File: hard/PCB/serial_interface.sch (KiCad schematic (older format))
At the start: 19 parts

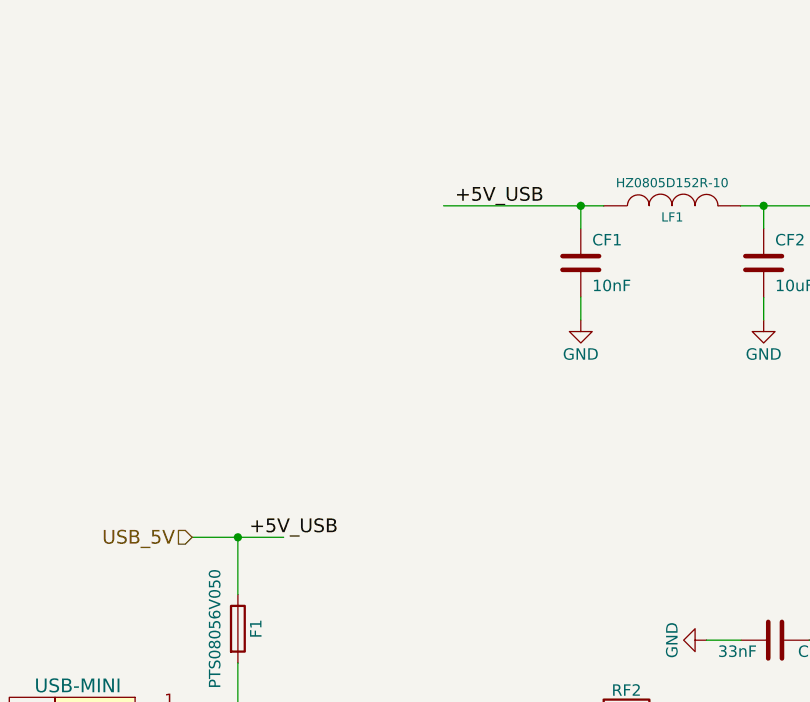
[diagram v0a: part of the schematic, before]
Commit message: se modifican el pin hdmi- las resitencias RN1 - eñ conector de  voltaje
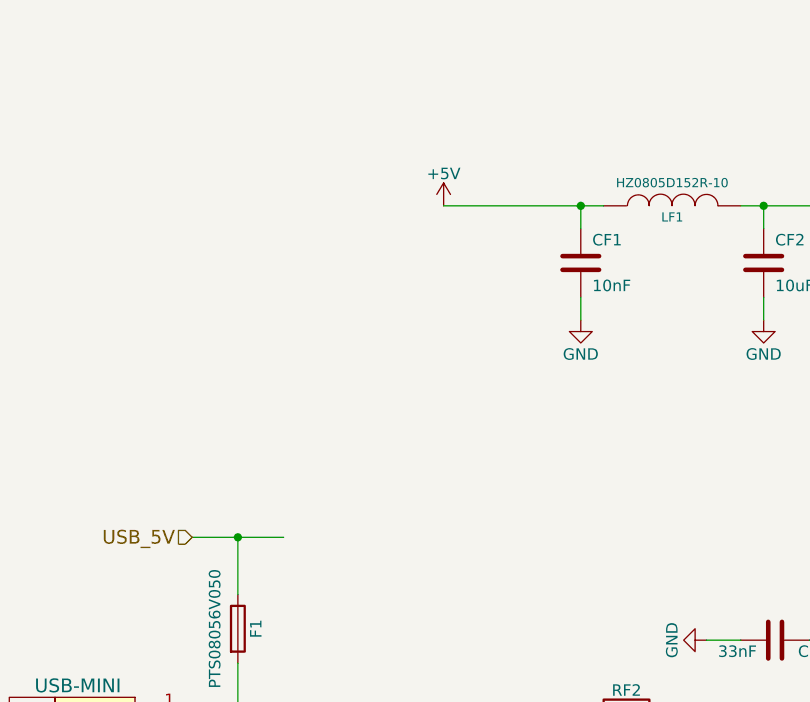
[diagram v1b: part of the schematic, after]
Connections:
- net labels added: +5V
- net labels removed: +5V_USB
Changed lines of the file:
@@
 Wire Wire Line
 	4750 3850 5150 3850
-Text Label 5000 3850 0    60   ~ 0
-+5V_USB
-Text Label 5900 2400 0    60   ~ 0
-+5V_USB
-Wire Wire Line
-	5850 2400 6550 2400
 $Comp
 L Fuse F1
@@
 Wire Wire Line
 	7600 6300 7400 6300
-Text Label 6800 6300 0    60   ~ 0
-+5VA
 Wire Wire Line
 	7600 5400 7200 5400
@@
 	0    1    1    0
 $EndComp
+Wire Wire Line
+	5850 2400 6550 2400
+$Comp
+L +5V #PWR019
+U 1 1 595DA814
+P 5850 2400
+F 0 "#PWR019" H 5850 2250 50  0001 C CNN
+F 1 "+5V" H 5850 2540 50  0000 C CNN
+F 2 "" H 5850 2400 50  0000 C CNN
+F 3 "" H 5850 2400 50  0000 C CNN
+	1    5850 2400
+	1    0    0    -1
+$EndComp
+Text Label 6800 6300 0    60   ~ 0
++5VA
 $EndSCHEMATC

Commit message: Changes in HDMISpartan6_Board
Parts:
- CF5, CF6: value 47pF -> 15pF
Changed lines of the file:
@@
 $Descr A3 16535 11693
 encoding utf-8
-Sheet 2 5
+Sheet 2 6
 Title ""
 Date "9 aug 2012"
@@
 P 5950 5500
 F 0 "CF5" H 6000 5600 50  0000 L CNN
-F 1 "47pF" V 6050 5250 50  0000 L CNN
+F 1 "15pF" V 6050 5250 50  0000 L CNN
 F 2 "Capacitors_SMD:C_0603" H 5950 5500 60  0001 C CNN
 F 3 "" H 5950 5500 60  0001 C CNN
@@
 P 5950 6100
 F 0 "CF6" H 6000 6200 50  0000 L CNN
-F 1 "47pF" V 6050 5850 50  0000 L CNN
+F 1 "15pF" V 6050 5850 50  0000 L CNN
 F 2 "Capacitors_SMD:C_0603" H 5950 6100 60  0001 C CNN
 F 3 "" H 5950 6100 60  0001 C CNN
@@
 $EndComp
 $Comp
-L +3V3 #PWR06
+L +3V3 #PWR010
 U 1 1 589F5460
 P 10300 6750
-F 0 "#PWR06" H 10300 6600 50  0001 C CNN
+F 0 "#PWR010" H 10300 6600 50  0001 C CNN
 F 1 "+3V3" H 10300 6890 50  0000 C CNN
 F 2 "" H 10300 6750 50  0000 C CNN
@@
 $EndComp
 $Comp
-L +3V3 #PWR07
+L +3V3 #PWR011
 U 1 1 589F5F40
 P 10300 5050
-F 0 "#PWR07" H 10300 4900 50  0001 C CNN
+F 0 "#PWR011" H 10300 4900 50  0001 C CNN
 F 1 "+3V3" H 10300 5190 50  0000 C CNN
 F 2 "" H 10300 5050 50  0000 C CNN
@@
 $EndComp
 $Comp
-L +3V3 #PWR08
+L +3V3 #PWR012
 U 1 1 589F6257
 P 10500 4800
-F 0 "#PWR08" H 10500 4650 50  0001 C CNN
+F 0 "#PWR012" H 10500 4650 50  0001 C CNN
 F 1 "+3V3" H 10500 4940 50  0000 C CNN
 F 2 "" H 10500 4800 50  0000 C CNN
@@
 $EndComp
 $Comp
-L +3V3 #PWR09
+L +3V3 #PWR013
 U 1 1 589F6BB3
 P 8800 3450
-F 0 "#PWR09" H 8800 3300 50  0001 C CNN
+F 0 "#PWR013" H 8800 3300 50  0001 C CNN
 F 1 "+3V3" H 8800 3590 50  0000 C CNN
 F 2 "" H 8800 3450 50  0000 C CNN
@@
 Wire Wire Line
 	7600 6400 7450 6400
-Connection ~ 8500 3450
-Wire Wire Line
-	8600 3700 8600 3450
-Wire Wire Line
-	8600 3450 8500 3450
 Wire Wire Line
 	8300 2900 8300 3700
@@
 Wire Wire Line
 	5050 4800 4800 4800
-Wire Wire Line
-	4800 5000 5000 5000
-Wire Wire Line
-	5000 5000 5000 5050
 Wire Wire Line
 	3650 4650 3650 5050
@@
 	6450 2500 6450 2400
 $Comp
-L GND #PWR010
+L GND #PWR014
 U 1 1 58A66750
 P 6450 2900
-F 0 "#PWR010" H 6450 2650 50  0001 C CNN
+F 0 "#PWR014" H 6450 2650 50  0001 C CNN
 F 1 "GND" H 6450 2750 50  0000 C CNN
 F 2 "" H 6450 2900 50  0000 C CNN
@@
 	7100 6300 6750 6300
 $Comp
-L GND #PWR011
+L GND #PWR015
 U 1 1 58A8D1C3
 P 7250 2900
-F 0 "#PWR011" H 7250 2650 50  0001 C CNN
+F 0 "#PWR015" H 7250 2650 50  0001 C CNN
 F 1 "GND" H 7250 2750 50  0000 C CNN
 F 2 "" H 7250 2900 50  0000 C CNN
@@
 $EndComp
 $Comp
-L GND #PWR012
+L GND #PWR016
 U 1 1 58A8D267
 P 7900 3350
-F 0 "#PWR012" H 7900 3100 50  0001 C CNN
+F 0 "#PWR016" H 7900 3100 50  0001 C CNN
 F 1 "GND" H 7900 3200 50  0000 C CNN
 F 2 "" H 7900 3350 50  0000 C CNN
@@
 $EndComp
 $Comp
-L GND #PWR013
+L GND #PWR017
 U 1 1 58A8D7DD
 P 8300 7400
-F 0 "#PWR013" H 8300 7150 50  0001 C CNN
+F 0 "#PWR017" H 8300 7150 50  0001 C CNN
 F 1 "GND" H 8300 7250 50  0000 C CNN
 F 2 "" H 8300 7400 50  0000 C CNN
@@
 $EndComp
 $Comp
-L GND #PWR014
+L GND #PWR018
 U 1 1 58A8DF8B
 P 7450 6450
-F 0 "#PWR014" H 7450 6200 50  0001 C CNN
+F 0 "#PWR018" H 7450 6200 50  0001 C CNN
 F 1 "GND" H 7450 6300 50  0000 C CNN
 F 2 "" H 7450 6450 50  0000 C CNN
@@
 $EndComp
 $Comp
-L GND #PWR015
+L GND #PWR019
 U 1 1 58A8E746
 P 5650 5900
-F 0 "#PWR015" H 5650 5650 50  0001 C CNN
+F 0 "#PWR019" H 5650 5650 50  0001 C CNN
 F 1 "GND" H 5650 5750 50  0000 C CNN
 F 2 "" H 5650 5900 50  0000 C CNN
@@
 $EndComp
 $Comp
-L GND #PWR016
+L GND #PWR020
 U 1 1 58A8EFD2
-P 5000 5050
-F 0 "#PWR016" H 5000 4800 50  0001 C CNN
-F 1 "GND" H 5000 4900 50  0000 C CNN
-F 2 "" H 5000 5050 50  0000 C CNN
-F 3 "" H 5000 5050 50  0000 C CNN
-	1    5000 5050
-	1    0    0    -1
-$EndComp
-$Comp
-L GND #PWR017
+P 4950 5050
+F 0 "#PWR020" H 4950 4800 50  0001 C CNN
+F 1 "GND" H 4950 4900 50  0000 C CNN
+F 2 "" H 4950 5050 50  0000 C CNN
+F 3 "" H 4950 5050 50  0000 C CNN
+	1    4950 5050
+	1    0    0    -1
+$EndComp
+$Comp
+L GND #PWR021
 U 1 1 58A8F696
 P 3650 5050
-F 0 "#PWR017" H 3650 4800 50  0001 C CNN
+F 0 "#PWR021" H 3650 4800 50  0001 C CNN
 F 1 "GND" H 3650 4900 50  0000 C CNN
 F 2 "" H 3650 5050 50  0000 C CNN
@@
 $EndComp
 $Comp
-L GND #PWR018
+L GND #PWR022
 U 1 1 58A8F991
 P 7000 4300
-F 0 "#PWR018" H 7000 4050 50  0001 C CNN
+F 0 "#PWR022" H 7000 4050 50  0001 C CNN
 F 1 "GND" H 7000 4150 50  0000 C CNN
 F 2 "" H 7000 4300 50  0000 C CNN
@@
 	5850 2400 6550 2400
 $Comp
-L +5V #PWR019
+L +5V #PWR023
 U 1 1 595DA814
 P 5850 2400
-F 0 "#PWR019" H 5850 2250 50  0001 C CNN
+F 0 "#PWR023" H 5850 2250 50  0001 C CNN
 F 1 "+5V" H 5850 2540 50  0000 C CNN
 F 2 "" H 5850 2400 50  0000 C CNN
@@
 Text Label 6800 6300 0    60   ~ 0
 +5VA
+Wire Wire Line
+	4950 5050 4950 5000
+Wire Wire Line
+	4950 5000 4800 5000
+Wire Wire Line
+	8600 3700 8600 3500
+Wire Wire Line
+	8600 3500 8500 3500
+Connection ~ 8500 3500
 $EndSCHEMATC
